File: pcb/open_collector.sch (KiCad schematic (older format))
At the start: 24 parts, among them Q1 Q_NPN_BCE, Q2 Q_NPN_BCE, Q3 Q_NPN_BCE, Q4 Q_NPN_BCE, Q5 Q_NPN_BCE, Q6 Q_NPN_BCE

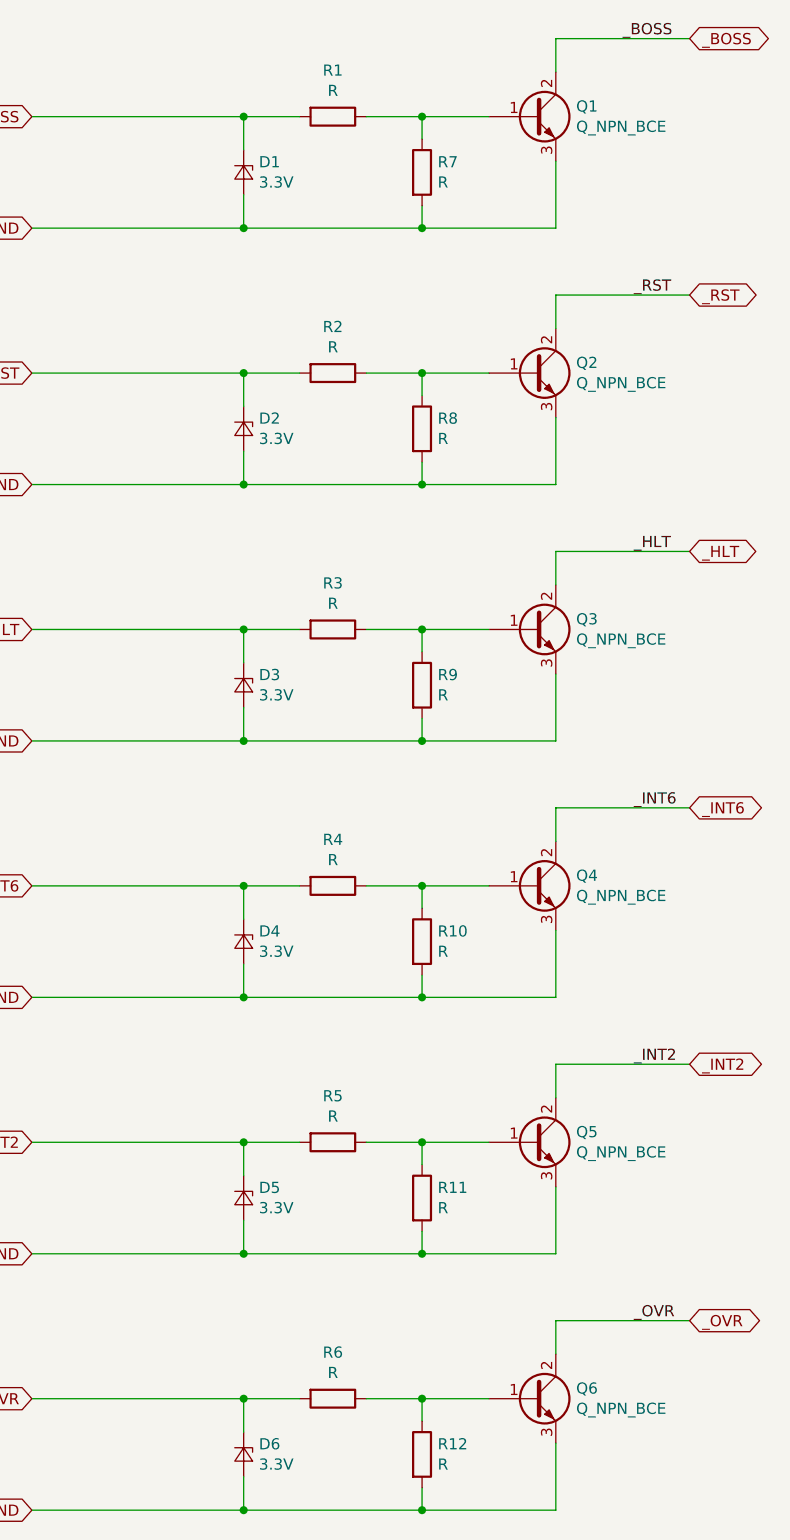
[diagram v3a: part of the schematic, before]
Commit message: fpga-side gpio connector added
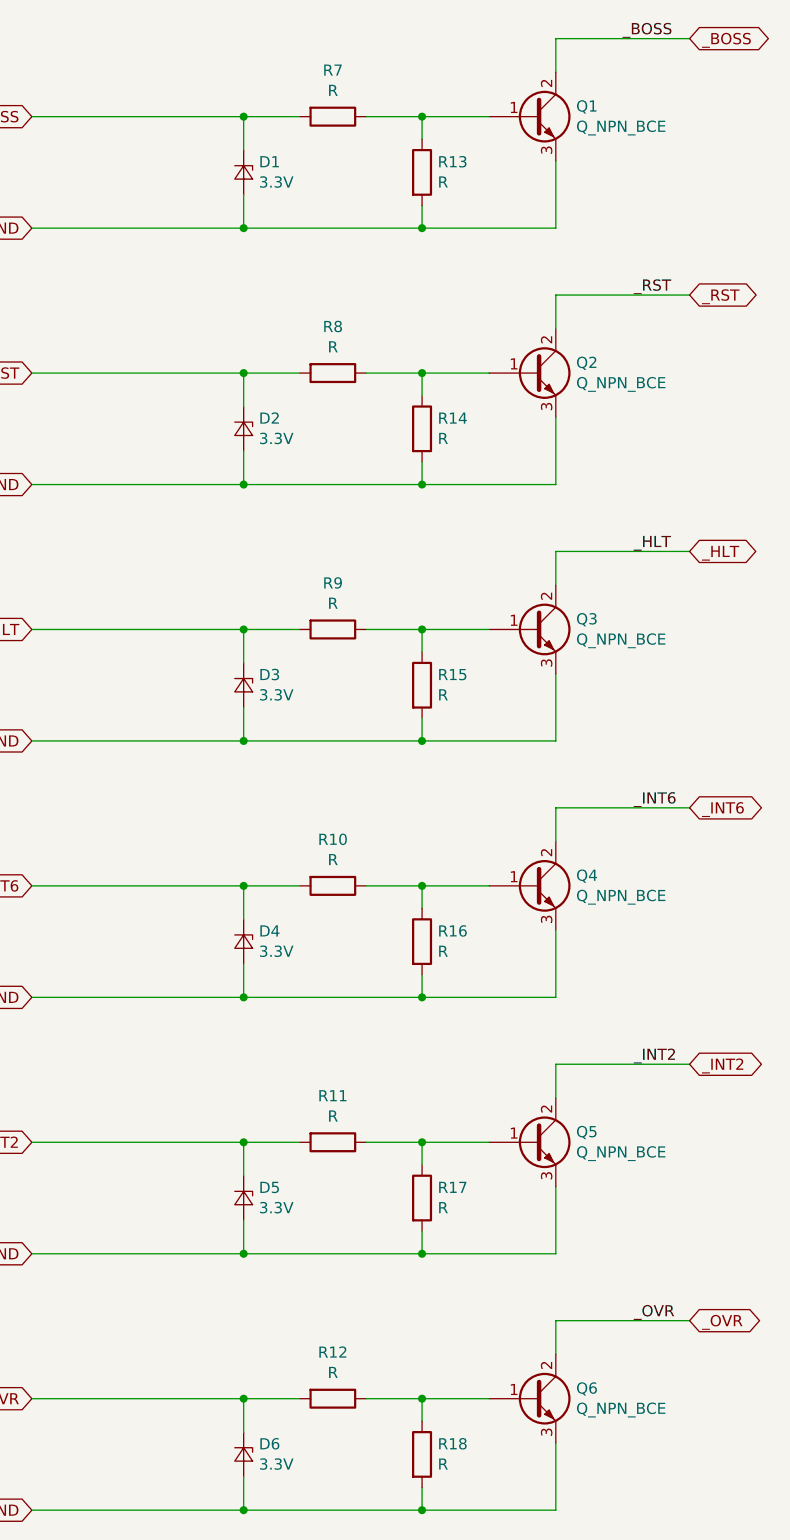
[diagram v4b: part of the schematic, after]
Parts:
- renumbered R4 to R10, R5 to R11, R6 to R12, R7 to R13, R8 to R14, R9 to R15, R10 to R16, R11 to R17, R12 to R18, R1 to R7, R2 to R8, R3 to R9
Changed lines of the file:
@@
 $EndComp
 $Comp
-L Device:R R1
+L Device:R R7
 U 1 1 5EB3731B
 P 2600 1200
-F 0 "R1" V 2393 1200 50  0000 C CNN
+F 0 "R7" V 2393 1200 50  0000 C CNN
 F 1 "R" V 2484 1200 50  0000 C CNN
 F 2 "" V 2530 1200 50  0001 C CNN
@@
 	3000 1300 3000 1200
 $Comp
-L Device:R R7
+L Device:R R13
 U 1 1 5EB387D5
 P 3000 1450
-F 0 "R7" H 3070 1496 50  0000 L CNN
+F 0 "R13" H 3070 1496 50  0000 L CNN
 F 1 "R" H 3070 1405 50  0000 L CNN
 F 2 "" V 2930 1450 50  0001 C CNN
@@
 $EndComp
 $Comp
-L Device:R R2
+L Device:R R8
 U 1 1 5EB4E153
 P 2600 2350
-F 0 "R2" V 2393 2350 50  0000 C CNN
+F 0 "R8" V 2393 2350 50  0000 C CNN
 F 1 "R" V 2484 2350 50  0000 C CNN
 F 2 "" V 2530 2350 50  0001 C CNN
@@
 	3000 2450 3000 2350
 $Comp
-L Device:R R8
+L Device:R R14
 U 1 1 5EB4E160
 P 3000 2600
-F 0 "R8" H 3070 2646 50  0000 L CNN
+F 0 "R14" H 3070 2646 50  0000 L CNN
 F 1 "R" H 3070 2555 50  0000 L CNN
 F 2 "" V 2930 2600 50  0001 C CNN
@@
 $EndComp
 $Comp
-L Device:R R3
+L Device:R R9
 U 1 1 5EB54613
 P 2600 3500
-F 0 "R3" V 2393 3500 50  0000 C CNN
+F 0 "R9" V 2393 3500 50  0000 C CNN
 F 1 "R" V 2484 3500 50  0000 C CNN
 F 2 "" V 2530 3500 50  0001 C CNN
@@
 	3000 3600 3000 3500
 $Comp
-L Device:R R9
+L Device:R R15
 U 1 1 5EB54620
 P 3000 3750
-F 0 "R9" H 3070 3796 50  0000 L CNN
+F 0 "R15" H 3070 3796 50  0000 L CNN
 F 1 "R" H 3070 3705 50  0000 L CNN
 F 2 "" V 2930 3750 50  0001 C CNN
@@
 $EndComp
 $Comp
-L Device:R R4
+L Device:R R10
 U 1 1 5EB574A7
 P 2600 4650
-F 0 "R4" V 2393 4650 50  0000 C CNN
+F 0 "R10" V 2393 4650 50  0000 C CNN
 F 1 "R" V 2484 4650 50  0000 C CNN
 F 2 "" V 2530 4650 50  0001 C CNN
@@
 	3000 4750 3000 4650
 $Comp
-L Device:R R10
+L Device:R R16
 U 1 1 5EB574B4
 P 3000 4900
-F 0 "R10" H 3070 4946 50  0000 L CNN
+F 0 "R16" H 3070 4946 50  0000 L CNN
 F 1 "R" H 3070 4855 50  0000 L CNN
 F 2 "" V 2930 4900 50  0001 C CNN
@@
 $EndComp
 $Comp
-L Device:R R5
+L Device:R R11
 U 1 1 5EB5A313
 P 2600 5800
-F 0 "R5" V 2393 5800 50  0000 C CNN
+F 0 "R11" V 2393 5800 50  0000 C CNN
 F 1 "R" V 2484 5800 50  0000 C CNN
 F 2 "" V 2530 5800 50  0001 C CNN
@@
 	3000 5900 3000 5800
 $Comp
-L Device:R R11
+L Device:R R17
 U 1 1 5EB5A320
 P 3000 6050
-F 0 "R11" H 3070 6096 50  0000 L CNN
+F 0 "R17" H 3070 6096 50  0000 L CNN
 F 1 "R" H 3070 6005 50  0000 L CNN
 F 2 "" V 2930 6050 50  0001 C CNN
@@
 $EndComp
 $Comp
-L Device:R R6
+L Device:R R12
 U 1 1 5EB5D164
 P 2600 6950
-F 0 "R6" V 2393 6950 50  0000 C CNN
+F 0 "R12" V 2393 6950 50  0000 C CNN
 F 1 "R" V 2484 6950 50  0000 C CNN
 F 2 "" V 2530 6950 50  0001 C CNN
@@
 	3000 7050 3000 6950
 $Comp
-L Device:R R12
+L Device:R R18
 U 1 1 5EB5D171
 P 3000 7200
-F 0 "R12" H 3070 7246 50  0000 L CNN
+F 0 "R18" H 3070 7246 50  0000 L CNN
 F 1 "R" H 3070 7155 50  0000 L CNN
 F 2 "" V 2930 7200 50  0001 C CNN

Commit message: Some more changes wip
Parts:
- added XT55, XT56, XT57, XT58, XT59, XT60: testpoint_cutline, symbol WM1200:testpoint_cutline
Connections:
- net FPGA_OC_BOSS: now also XT55.1 (A); no longer D1.1 (K), R7.2
- net FPGA_OC_HLT: now also XT57.1 (A); no longer D3.1 (K), R9.2
- net FPGA_OC_INT2: now also XT59.1 (A); no longer D5.1 (K), R11.2
- net FPGA_OC_INT6: now also XT58.1 (A); no longer D4.1 (K), R10.2
- net FPGA_OC_OVR: now also XT60.1 (A); no longer D6.1 (K), R12.2
- net FPGA_OC_RST: now also XT56.1 (A); no longer D2.1 (K), R8.2
- new net: D6.1 (K), R12.2, XT60.2 (B)
- new net: D5.1 (K), R11.2, XT59.2 (B)
- new net: D4.1 (K), R10.2, XT58.2 (B)
- new net: D3.1 (K), R9.2, XT57.2 (B)
- new net: D2.1 (K), R8.2, XT56.2 (B)
- new net: D1.1 (K), R7.2, XT55.2 (B)
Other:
- note added: "Don't forget about pull-ups and pull-downs"
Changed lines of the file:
@@
 $Descr A4 11693 8268
 encoding utf-8
-Sheet 3 11
+Sheet 10 11
 Title "WishMaster 1200"
 Date ""
@@
 $EndComp
 Wire Wire Line
-	1250 1200 2200 1200
-Wire Wire Line
 	4200 850  3600 850
 Wire Wire Line
@@
 Wire Wire Line
 	2200 1200 2200 1350
-Connection ~ 2200 1200
 Wire Wire Line
 	2200 1200 2450 1200
@@
 $EndComp
 Wire Wire Line
-	1250 2350 2200 2350
-Wire Wire Line
 	4200 2000 3600 2000
 Wire Wire Line
@@
 Wire Wire Line
 	2200 2350 2200 2500
-Connection ~ 2200 2350
 Wire Wire Line
 	2200 2350 2450 2350
@@
 $EndComp
 Wire Wire Line
-	1250 3500 2200 3500
-Wire Wire Line
 	4200 3150 3600 3150
 Wire Wire Line
@@
 Wire Wire Line
 	2200 3500 2200 3650
-Connection ~ 2200 3500
 Wire Wire Line
 	2200 3500 2450 3500
@@
 $EndComp
 Wire Wire Line
-	1250 4650 2200 4650
-Wire Wire Line
 	4200 4300 3600 4300
 Wire Wire Line
@@
 Wire Wire Line
 	2200 4650 2200 4800
-Connection ~ 2200 4650
 Wire Wire Line
 	2200 4650 2450 4650
@@
 $EndComp
 Wire Wire Line
-	1250 5800 2200 5800
-Wire Wire Line
 	4200 5450 3600 5450
 Wire Wire Line
@@
 Wire Wire Line
 	2200 5800 2200 5950
-Connection ~ 2200 5800
 Wire Wire Line
 	2200 5800 2450 5800
@@
 $EndComp
 Wire Wire Line
-	1250 6950 2200 6950
-Wire Wire Line
 	4200 6600 3600 6600
 Wire Wire Line
@@
 Wire Wire Line
 	2200 6950 2200 7100
-Connection ~ 2200 6950
 Wire Wire Line
 	2200 6950 2450 6950
@@
 Text GLabel 4200 6600 2    50   BiDi ~ 0
 _OVR
+$Comp
+L WM1200:testpoint_cutline XT60
+U 1 1 5E66C58B
+P 1700 7000
+F 0 "XT60" H 1700 7183 50  0000 C CNN
+F 1 "testpoint_cutline" H 1700 7150 50  0001 C CNN
+F 2 "" H 1850 7000 50  0001 C CNN
+F 3 "" H 1850 7000 50  0001 C CNN
+	1    1700 7000
+	1    0    0    -1
+$EndComp
+$Comp
+L WM1200:testpoint_cutline XT59
+U 1 1 5E66D323
+P 1700 5850
+F 0 "XT59" H 1700 6033 50  0000 C CNN
+F 1 "testpoint_cutline" H 1700 6000 50  0001 C CNN
+F 2 "" H 1850 5850 50  0001 C CNN
+F 3 "" H 1850 5850 50  0001 C CNN
+	1    1700 5850
+	1    0    0    -1
+$EndComp
+$Comp
+L WM1200:testpoint_cutline XT58
+U 1 1 5E66DA82
+P 1700 4700
+F 0 "XT58" H 1700 4883 50  0000 C CNN
+F 1 "testpoint_cutline" H 1700 4850 50  0001 C CNN
+F 2 "" H 1850 4700 50  0001 C CNN
+F 3 "" H 1850 4700 50  0001 C CNN
+	1    1700 4700
+	1    0    0    -1
+$EndComp
+$Comp
+L WM1200:testpoint_cutline XT57
+U 1 1 5E66DF74
+P 1700 3550
+F 0 "XT57" H 1700 3733 50  0000 C CNN
+F 1 "testpoint_cutline" H 1700 3700 50  0001 C CNN
+F 2 "" H 1850 3550 50  0001 C CNN
+F 3 "" H 1850 3550 50  0001 C CNN
+	1    1700 3550
+	1    0    0    -1
+$EndComp
+$Comp
+L WM1200:testpoint_cutline XT56
+U 1 1 5E66E467
+P 1700 2400
+F 0 "XT56" H 1700 2583 50  0000 C CNN
+F 1 "testpoint_cutline" H 1700 2550 50  0001 C CNN
+F 2 "" H 1850 2400 50  0001 C CNN
+F 3 "" H 1850 2400 50  0001 C CNN
+	1    1700 2400
+	1    0    0    -1
+$EndComp
+$Comp
+L WM1200:testpoint_cutline XT55
+U 1 1 5E66EAB6
+P 1700 1250
+F 0 "XT55" H 1700 1433 50  0000 C CNN
+F 1 "testpoint_cutline" H 1700 1400 50  0001 C CNN
+F 2 "" H 1850 1250 50  0001 C CNN
+F 3 "" H 1850 1250 50  0001 C CNN
+	1    1700 1250
+	1    0    0    -1
+$EndComp
+Wire Wire Line
+	1300 1200 1250 1200
+Wire Wire Line
+	2100 1200 2200 1200
+Connection ~ 2200 1200
+Wire Wire Line
+	2100 2350 2200 2350
+Connection ~ 2200 2350
+Wire Wire Line
+	1300 2350 1250 2350
+Wire Wire Line
+	1250 3500 1300 3500
+Wire Wire Line
+	2100 3500 2200 3500
+Connection ~ 2200 3500
+Wire Wire Line
+	1250 4650 1300 4650
+Wire Wire Line
+	2100 4650 2200 4650
+Connection ~ 2200 4650
+Wire Wire Line
+	1250 5800 1300 5800
+Wire Wire Line
+	2100 5800 2200 5800
+Connection ~ 2200 5800
+Wire Wire Line
+	1250 6950 1300 6950
+Wire Wire Line
+	2100 6950 2200 6950
+Connection ~ 2200 6950
+Text Notes 4300 3900 0    118  Italic 24
+Don't forget about pull-ups and pull-downs
 $EndSCHEMATC

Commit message: open collector list finished
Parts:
- removed Q1, Q2, Q3, Q4, Q5, Q6: Q_NPN_BCE, symbol Device:Q_NPN_BCE
- added Q1, Q2, Q3, Q4, Q5, Q6: BC817, Package_TO_SOT_SMD:SOT-23, symbol Transistor_BJT:BC817
- added R16, R20: 1k, symbol Device:R
- added XT59, XT60, XT61, XT62, XT65, XT66: testpoint_cutline, symbol WM1200:testpoint_cutline
- R10: renamed from R12; value R -> 1k
- R11: renamed from R15; value R -> 1k
- R12: renamed from R16; value R -> 1k
- R13: renamed from R17; value R -> 1k
- R14: renamed from R18; value R -> 1k
- R15: renamed from R14; value R -> 1k
- R17: renamed from R8; value R -> 1k
- R18: renamed from R7; value R -> 1k
- R19: renamed from R13; value R -> 1k
- R7: renamed from R9; value R -> 1k
- R8: renamed from R10; value R -> 1k
- R9: renamed from R11; value R -> 1k
- renumbered D3 to D1, D4 to D2, D5 to D3, D6 to D4, D2 to D5, D1 to D6, XT57 to XT55, XT58 to XT56, XT59 to XT57, XT60 to XT58, XT56 to XT63, XT55 to XT64
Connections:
- net labels added: +3V3_BUFFER
- wire segments 90 -> 102
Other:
- note added: "opened by default"
- note added: "tied to gnd by default"
- note added: "use either one of those resistors\n(pullup or pulldown)"
- moved on the sheet: D1, D2, D3, D4, D5, D6, R10, R11, R12, R13, R14, R15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

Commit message: changed pullup resistance and zener diodes voltage at OC list
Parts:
- D1, D2, D3, D4, D5, D6: value 3.3V -> 3.5V
- R15, R16: value 1k -> 4.7k
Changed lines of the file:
@@
 P 7650 2100
 F 0 "D6" V 7604 2168 50  0000 L CNN
-F 1 "3.3V" V 7695 2168 50  0000 L CNN
+F 1 "3.5V" V 7695 2168 50  0000 L CNN
 F 2 "" V 7650 2100 50  0001 C CNN
 F 3 "~" V 7650 2100 50  0001 C CNN
@@
 P 7600 3550
 F 0 "R15" H 7670 3596 50  0000 L CNN
-F 1 "1k" H 7670 3505 50  0000 L CNN
+F 1 "4.7k" H 7670 3505 50  0000 L CNN
 F 2 "" V 7530 3550 50  0001 C CNN
 F 3 "~" H 7600 3550 50  0001 C CNN
@@
 P 7600 4100
 F 0 "D5" V 7554 4168 50  0000 L CNN
-F 1 "3.3V" V 7645 4168 50  0000 L CNN
+F 1 "3.5V" V 7645 4168 50  0000 L CNN
 F 2 "" V 7600 4100 50  0001 C CNN
 F 3 "~" V 7600 4100 50  0001 C CNN
@@
 P 2100 1750
 F 0 "D1" V 2054 1818 50  0000 L CNN
-F 1 "3.3V" V 2145 1818 50  0000 L CNN
+F 1 "3.5V" V 2145 1818 50  0000 L CNN
 F 2 "" V 2100 1750 50  0001 C CNN
 F 3 "~" V 2100 1750 50  0001 C CNN
@@
 P 2100 3250
 F 0 "D2" V 2054 3318 50  0000 L CNN
-F 1 "3.3V" V 2145 3318 50  0000 L CNN
+F 1 "3.5V" V 2145 3318 50  0000 L CNN
 F 2 "" V 2100 3250 50  0001 C CNN
 F 3 "~" V 2100 3250 50  0001 C CNN
@@
 	1    0    0    -1
 $EndComp
-$Comp
-L Device:D_Zener_Small D3
-U 1 1 5EB5A326
-P 2100 4750
-F 0 "D3" V 2054 4818 50  0000 L CNN
-F 1 "3.3V" V 2145 4818 50  0000 L CNN
-F 2 "" V 2100 4750 50  0001 C CNN
-F 3 "~" V 2100 4750 50  0001 C CNN
-	1    2100 4750
-	0    1    1    0
-$EndComp
 Wire Wire Line
 	2650 4500 2900 4500
@@
 P 2100 6250
 F 0 "D4" V 2054 6318 50  0000 L CNN
-F 1 "3.3V" V 2145 6318 50  0000 L CNN
+F 1 "3.5V" V 2145 6318 50  0000 L CNN
 F 2 "" V 2100 6250 50  0001 C CNN
 F 3 "~" V 2100 6250 50  0001 C CNN
@@
 P 7650 1600
 F 0 "R16" H 7720 1646 50  0000 L CNN
-F 1 "1k" H 7720 1555 50  0000 L CNN
+F 1 "4.7k" H 7720 1555 50  0000 L CNN
 F 2 "" V 7580 1600 50  0001 C CNN
 F 3 "~" H 7650 1600 50  0001 C CNN
@@
 Text Notes 7850 3500 0    50   ~ 0
 use either one of those resistors\n(pullup or pulldown)
+$Comp
+L Device:D_Zener_Small D3
+U 1 1 5EB5A326
+P 2100 4750
+F 0 "D3" V 2054 4818 50  0000 L CNN
+F 1 "3.5V" V 2145 4818 50  0000 L CNN
+F 2 "" V 2100 4750 50  0001 C CNN
+F 3 "~" V 2100 4750 50  0001 C CNN
+	1    2100 4750
+	0    1    1    0
+$EndComp
 $EndSCHEMATC
